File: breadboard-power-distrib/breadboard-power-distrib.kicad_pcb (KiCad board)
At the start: 2 copper layers, 40 x 35.6 mm, 6 parts, among them J1 +V/GND, J2 -V/GND, J3 +V, J4 GND, J5 -V

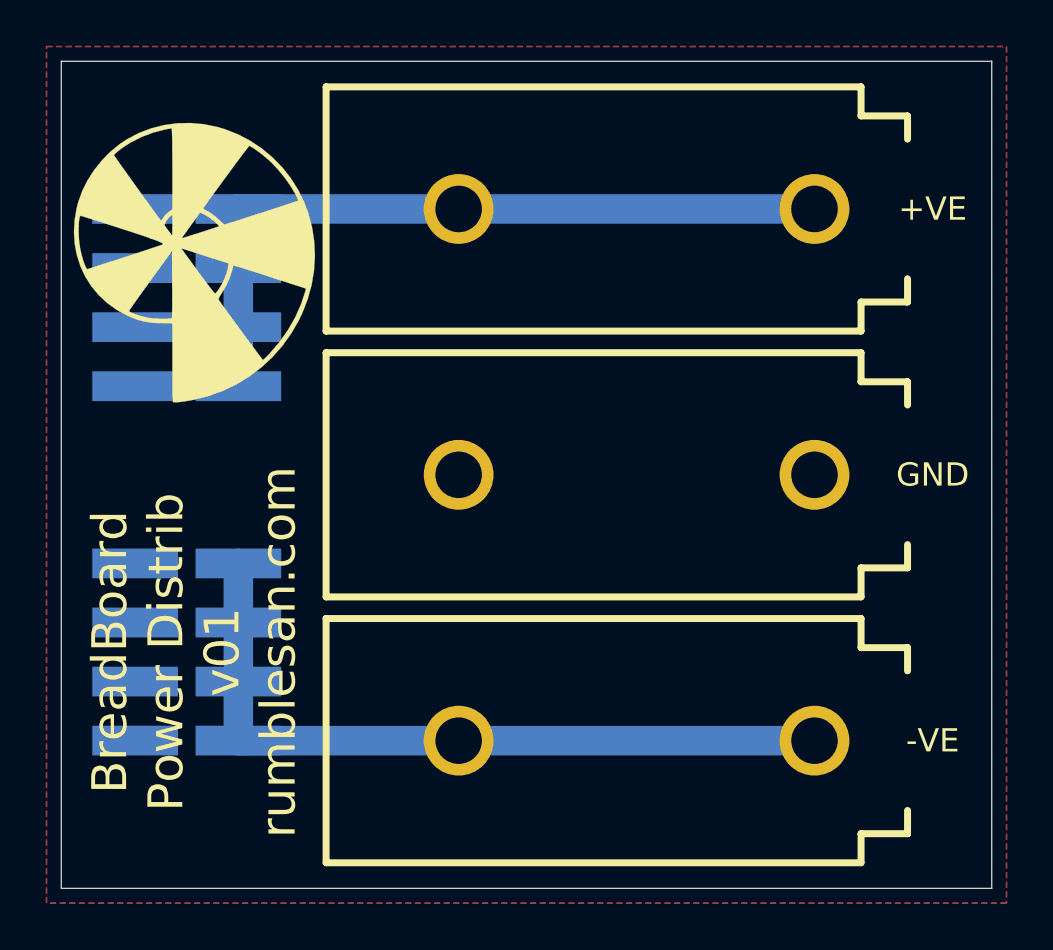
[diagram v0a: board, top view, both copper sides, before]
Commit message: breadboard power distrib tweaks
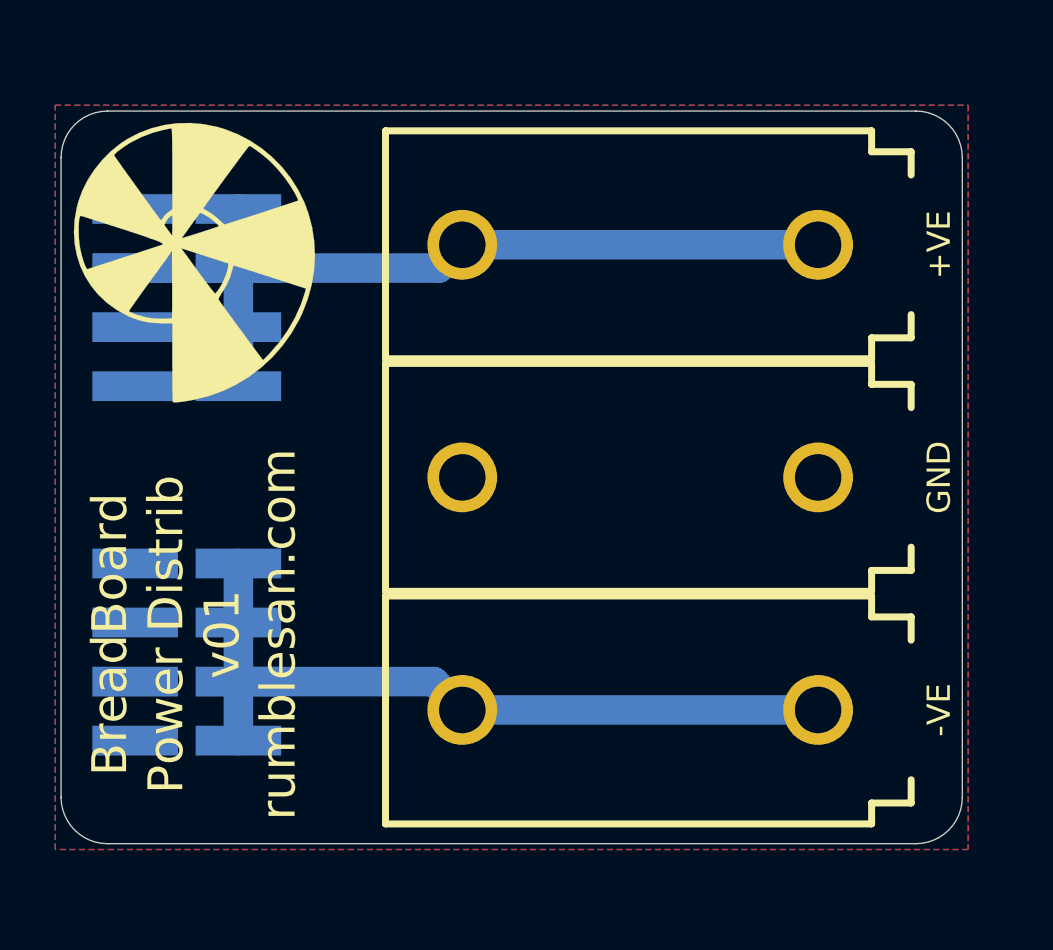
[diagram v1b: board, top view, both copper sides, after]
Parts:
- moved J3 1.55 mm to (112.5, 62.5)
- moved J5 1.33 mm to (112.5, 82.5)
- moved J4 0.19 mm to (112.5, 72.5)
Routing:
- net Net-(J2-Pad5): track 32.4 -> 33.1 mm
- net Net-(J1-Pad5): track 32.4 -> 33.0 mm
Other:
- board size 40 x 35.6 mm -> 38.8 x 31.5 mm

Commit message: Updating ordered boards
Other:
- rule pad_to_mask_clearance: 0.0508 -> 0
